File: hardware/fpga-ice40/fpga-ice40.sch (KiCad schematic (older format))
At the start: 70 parts, among them J1 MicroSD_Molex_1040310811, J4 Conn_02x20_Odd_Even, J5 USB_B_Micro, J6 Conn_02x05_Odd_Even, J7 Conn_02x05_Odd_Even, U1 iCE40HX4K-TQ144, U2 IS42S16320F-6TL, U3 W25Q32JVSS, U4 W25Q32JVSS, U5 S25FL256SAGMFI01, U6 S25FL256SAGMFI01, U7 FT245RL, U8 AZ1117-1.2, U9 AZ1117-1.2

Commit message: Oscillator, LEDs implemented, with all traces routed roughly
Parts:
- added C39, C40, C42: 10n, Capacitor_SMD:C_0603_1608Metric, symbol Device:C
- added C41, C43: 100n, Capacitor_SMD:C_0603_1608Metric, symbol Device:C
- added D2, D3, D4, D5, D6: Blue, LED_SMD:LED_0603_1608Metric, symbol Device:LED
- added FB1: 33R, 500mA, Inductor_SMD:L_0603_1608Metric, symbol Device:Ferrite_Bead
- added J2: Conn_01x03, Connector_PinHeader_2.54mm:PinHeader_1x03_P2.54mm_Vertical, symbol Connector_Generic:Conn_01x03
- added Q1: 2N7002H, Package_TO_SOT_SMD:SOT-23, symbol Transistor_FET:2N7002H
- added R5: 470R, Resistor_SMD:R_0603_1608Metric, symbol Device:R
- added R6: 100k, Resistor_SMD:R_0603_1608Metric, symbol Device:R
- added R7: 330R, Resistor_SMD:R_Array_Convex_4x0603, symbol Device:R_Pack04_Split
- added X1: ECS-2520MV-xxx-xx, Oscillator:Oscillator_SMD_ECS_2520MV-xxx-xx-4Pin_2.5x2.0mm, symbol Oscillator:ECS-2520MV-xxx-xx
- C27: footprint Capacitor_SMD:C_0603_1608Metric -> Capacitor_SMD:C_0805_2012Metric
- D1: value D_Schottky -> ~~800mVf; footprint (none) -> Diode_SMD:D_SOD-123
- RN4, RN5, RN6, RN7, RN8, RN9: value 33R0 -> 33R
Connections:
- net DRAM_DQ3: now also U1.2 (IOL_2B); no longer U1.141 (IOT_219)
- net DRAM_DQ4: now also U1.141 (IOT_219); no longer U1.2 (IOL_2B)
- net FIFO_D0: now also U1.105 (IOR_165); no longer U1.107 (IOR_167)
- net FIFO_D1: now also U1.101 (IOR_160); no longer U1.102 (IOR_161)
- net FIFO_D2: now also U1.102 (IOR_161); no longer U1.105 (IOR_165)
- net FIFO_D3: now also U1.94 (IOR_141_GBIN2); no longer U1.95 (IOR_144)
- net FIFO_D4: now also U1.104 (IOR_164); no longer U1.106 (IOR_166)
- net FIFO_D7: now also U1.99 (IOR_152); no longer U1.101 (IOR_160)
- net FIFO_RDn: now also U1.91 (IOR_139); no longer U1.94 (IOR_141_GBIN2)
- net FIFO_RXFn: now also U1.98 (IOR_148); no longer U1.104 (IOR_164)
- net FIFO_TXEn: now also U1.95 (IOR_144); no longer U1.99 (IOR_152)
- net FIFO_WR: now also U1.90 (IOR_138); no longer U1.93 (IOR_140_GBIN3)
- net FPGA_CDONE: now also Q1.1 (G)
- net GND: now also C39.2, C40.2, C41.2, C42.2, C43.2, D3.1 (K), D4.1 (K), D5.1 (K), D6.1 (K), Q1.2 (S), R6.1, X1.2 (GND)
- net N64_3V3: now also J2.1 (Pin_1)
- net N64_AD0_IC: now also U1.107 (IOR_167); no longer U1.112 (IOT_169)
- net N64_AD10_IC: now also U1.121 (IOT_181); no longer U1.128 (IOT_197_GBIN1)
- net N64_AD11_IC: now also U1.125 (IOT_192); no longer U1.124 (IOT_191)
- net N64_AD12_IC: now also U1.115 (IOT_172); no longer U1.117 (IOT_174)
- net N64_AD13_IC: now also U1.113 (IOT_170); no longer U1.115 (IOT_172)
- net N64_AD14_IC: now also U1.112 (IOT_169); no longer U1.110 (IOT_168)
- net N64_AD15_IC: now also U1.106 (IOR_166); no longer U1.113 (IOT_170)
- net N64_AD1_IC: now also U1.110 (IOT_168); no longer U1.114 (IOT_171)
- net N64_AD2_IC: now also U1.114 (IOT_171); no longer U1.116 (IOT_173)
- net N64_AD3_IC: now also U1.116 (IOT_173); no longer U1.118 (IOT_177)
- net N64_AD4_IC: now also U1.124 (IOT_191); no longer U1.125 (IOT_192)
- net N64_AD5_IC: now also U1.122 (IOT_190); no longer U1.129 (IOT_198_GBIN0)
- net N64_AD6: now also RN8.1 (R1.1); no longer RN8.2 (R2.1)
- net N64_AD6_IC: now also RN8.8 (R1.2), U1.130 (IOT_206); no longer RN8.7 (R2.2), U1.134 (IOT_212)
- net N64_AD7: now also RN8.3 (R3.1); no longer RN8.4 (R4.1)
- net N64_AD7_IC: now also RN8.6 (R3.2), U1.135 (IOT_213); no longer RN8.5 (R4.2), U1.136 (IOT_214)
- net N64_AD8: now also RN8.4 (R4.1); no longer RN8.3 (R3.1)
- net N64_AD8_IC: now also RN8.5 (R4.2), U1.136 (IOT_214); no longer RN8.6 (R3.2), U1.135 (IOT_213)
- net N64_AD9: now also RN8.2 (R2.1); no longer RN8.1 (R1.1)
- net N64_AD9_IC: now also RN8.7 (R2.2), U1.134 (IOT_212); no longer RN8.8 (R1.2), U1.130 (IOT_206)
- net N64_ALE_H_IC: now also U1.117 (IOT_174); no longer U1.122 (IOT_190)
- net N64_ALE_L: now also RN6.1 (R1.1); no longer RN6.2 (R2.1)
- net N64_ALE_L_IC: now also RN6.8 (R1.2); no longer RN6.7 (R2.2)
- net N64_COLD_RESETn: now also RN9.2 (R2.1); no longer RN9.1 (R1.1)
- net N64_COLD_RESETn_IC: now also RN9.7 (R2.2), U1.138 (IOT_216); no longer RN9.8 (R1.2), U1.137 (IOT_215)
- net N64_OS_EVENTn: now also RN9.1 (R1.1); no longer RN9.2 (R2.1)
- net N64_OS_EVENTn_IC: now also RN9.8 (R1.2), U1.137 (IOT_215); no longer RN9.7 (R2.2), U1.138 (IOT_216)
- net N64_READn_IC: now also U1.118 (IOT_177); no longer U1.121 (IOT_181)
- net N64_WRITEn: now also RN6.2 (R2.1); no longer RN6.1 (R1.1)
- net N64_WRITEn_IC: now also RN6.7 (R2.2); no longer RN6.8 (R1.2)
- net P3V3: now also C43.1, J2.2 (Pin_2), R5.1, X1.1 (Tri-State), X1.4 (VDD)
- net SD_CLK: now also U1.75 (IOR_111)
- net SD_CMD: now also RN3.3 (R3.1), U1.76 (IOR_112); no longer RN3.2 (R2.1)
- net SD_DAT0: now also RN3.2 (R2.1), U1.74 (IOR_110); no longer RN3.3 (R3.1)
- net SD_DAT1: now also RN3.1 (R1.1), U1.73 (IOR_109); no longer RN3.4 (R4.1)
- net SD_DAT2: now also U1.79 (IOR_115)
- net SD_DAT3: now also RN3.4 (R4.1), U1.78 (IOR_114); no longer RN3.1 (R1.1)
- net USB_3V3: now also J2.3 (Pin_3)
- net USB_DETn: now also U1.93 (IOR_140_GBIN3); no longer U1.98 (IOR_148)
- net USB_VBUS: now also C39.1, FB1.2; no longer C34.1, R3.1, U7.20 (VCC), U8.3 (VI)
- net SD_CD: now reaches U1.80 (IOR_116)
- net SD_CD: now also J1.9 (Pin_9)
- net LED_D0: now reaches U1.81 (IOR_117)
- net LED_D0: now also R7.5
- net LED_D1: now reaches U1.82 (IOR_118)
- net LED_D1: now also R7.6
- net LED_D2: now reaches U1.83 (IOR_119)
- net LED_D2: now also R7.7
- net LED_D3: now reaches U1.84 (IOR_120)
- net LED_D3: now also R7.8
- net USB_SHD: now reaches J5.6 (Shield)
- net USB_SHD: now also C42.1, R6.2
- new net: D2.1 (K), Q1.3 (D)
- new net: D2.2 (A), R5.2
- new net: D3.2 (A), R7.4
- new net: D6.2 (A), R7.1
- new net: D4.2 (A), R7.3
- new net: D5.2 (A), R7.2
- new net CLK_50MHZ: U1.128 (IOT_197_GBIN1), X1.3 (OUT)
- new net USB_5V: C34.1, C40.1, C41.1, FB1.1, R3.1, U7.20 (VCC), U8.3 (VI)
- no-connect marks 23 -> 29
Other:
- moved on the sheet: C33, C34, C35, C36, R3, R4, R9, U7, U8

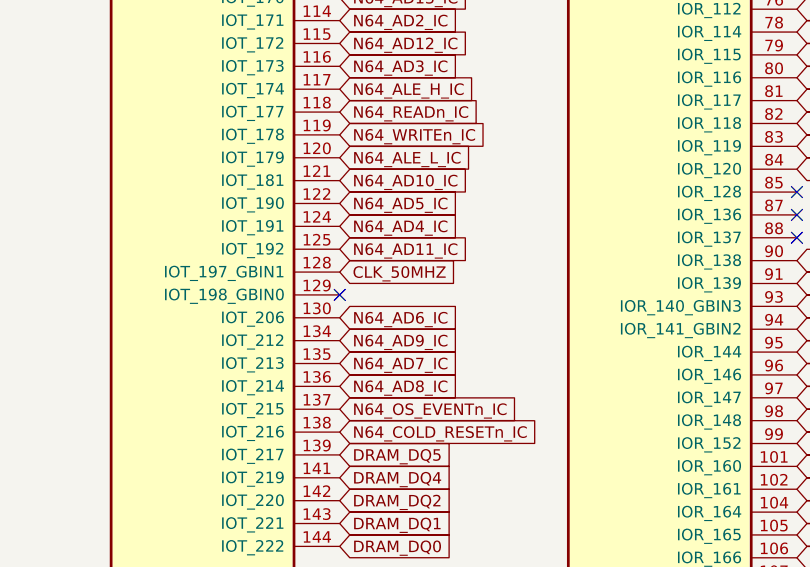
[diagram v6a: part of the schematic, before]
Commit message: Reroute N64 AD cart net away from clock oscillator output net
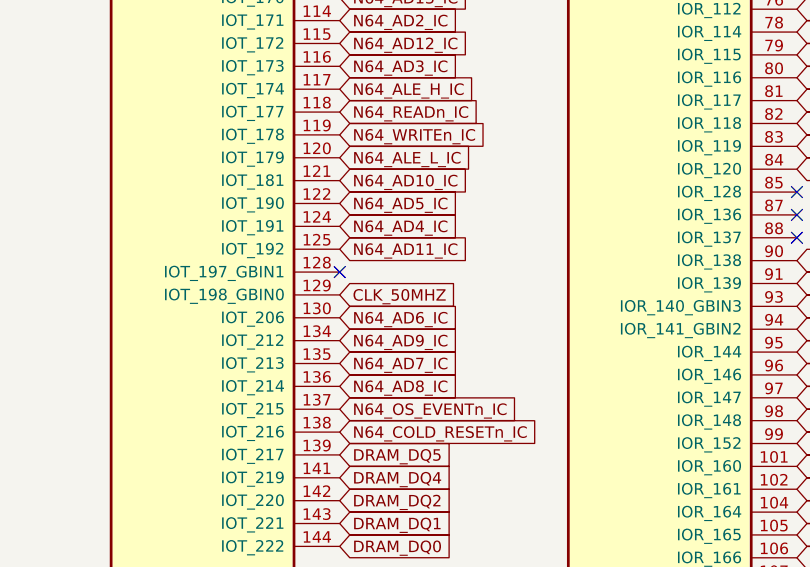
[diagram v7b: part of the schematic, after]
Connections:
- net CLK_50MHZ: now also U1.129 (IOT_198_GBIN0); no longer U1.128 (IOT_197_GBIN1)
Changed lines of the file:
@@
 Text GLabel 15200 3000 2    50   Input ~ 0
 CLK_50MHZ
-Text GLabel 2500 3000 2    50   Input ~ 0
+Text GLabel 2500 3100 2    50   Input ~ 0
 CLK_50MHZ
-NoConn ~ 2500 3100
+NoConn ~ 2500 3000
 NoConn ~ 4500 2650
 NoConn ~ 4500 2750

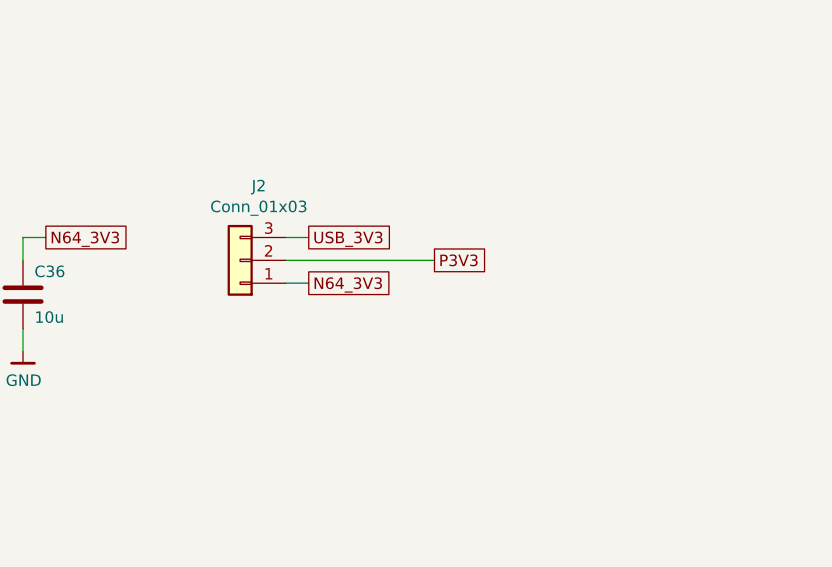
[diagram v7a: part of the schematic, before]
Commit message: Completed first pass routing with DRC checks passing
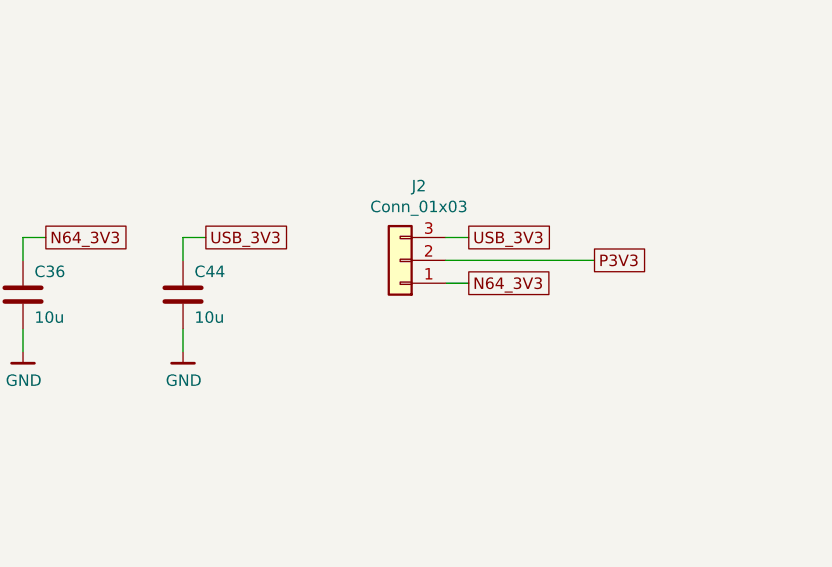
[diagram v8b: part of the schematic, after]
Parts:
- added C44: 10u, Capacitor_SMD:C_0805_2012Metric, symbol Device:C
- U3, U4: footprint Package_SO:SOIC-8_5.275x5.275mm_P1.27mm -> local_hacks:SOIC-8_5.275x5.275mm_P1.27mm__No_CrtYd
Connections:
- net GND: now also C44.2
- net USB_3V3: now also C44.1
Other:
- moved on the sheet: J2
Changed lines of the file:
@@
 F 0 "U3" H 18550 6750 50  0000 R CNN
 F 1 "W25Q32JVSS" H 18550 6650 50  0000 R CNN
-F 2 "Package_SO:SOIC-8_5.275x5.275mm_P1.27mm" H 18150 5750 50  0001 C CNN
+F 2 "local_hacks:SOIC-8_5.275x5.275mm_P1.27mm__No_CrtYd" H 18150 5750 50  0001 C CNN
 F 3 "https://www.mouser.com/datasheet/2/949/w25q32jv_dtr_revg_03272018_plus-1489786.pdf" H 18650 6300 50  0001 C CNN
 	1    17650 6600
@@
 F 0 "U4" H 18550 8850 50  0000 R CNN
 F 1 "W25Q32JVSS" H 18550 8750 50  0000 R CNN
-F 2 "Package_SO:SOIC-8_5.275x5.275mm_P1.27mm" H 18150 7850 50  0001 C CNN
+F 2 "local_hacks:SOIC-8_5.275x5.275mm_P1.27mm__No_CrtYd" H 18150 7850 50  0001 C CNN
 F 3 "https://www.mouser.com/datasheet/2/949/w25q32jv_dtr_revg_03272018_plus-1489786.pdf" H 18650 8400 50  0001 C CNN
 	1    17650 8700
@@
 L Connector_Generic:Conn_01x03 J2
 U 1 1 6261B7B7
-P 5050 11100
-F 0 "J2" H 4968 10775 50  0000 C CNN
-F 1 "Conn_01x03" H 4968 10866 50  0000 C CNN
-F 2 "Connector_PinHeader_2.54mm:PinHeader_1x03_P2.54mm_Vertical" H 5050 11100 50  0001 C CNN
-F 3 "~" H 5050 11100 50  0001 C CNN
-	1    5050 11100
+P 5750 11100
+F 0 "J2" H 5668 10775 50  0000 C CNN
+F 1 "Conn_01x03" H 5668 10866 50  0000 C CNN
+F 2 "Connector_PinHeader_2.54mm:PinHeader_1x03_P2.54mm_Vertical" H 5750 11100 50  0001 C CNN
+F 3 "~" H 5750 11100 50  0001 C CNN
+	1    5750 11100
 	-1   0    0    1
 $EndComp
 Wire Wire Line
-	5250 11000 5350 11000
-Wire Wire Line
-	5250 11100 5900 11100
-Wire Wire Line
-	5250 11200 5350 11200
-Text GLabel 5350 11000 2    50   UnSpc ~ 0
+	5950 11000 6050 11000
+Wire Wire Line
+	5950 11100 6600 11100
+Wire Wire Line
+	5950 11200 6050 11200
+Text GLabel 6050 11000 2    50   UnSpc ~ 0
 USB_3V3
-Text GLabel 5350 11200 2    50   UnSpc ~ 0
+Text GLabel 6050 11200 2    50   UnSpc ~ 0
 N64_3V3
-Text GLabel 5900 11100 2    50   UnSpc ~ 0
+Text GLabel 6600 11100 2    50   UnSpc ~ 0
 P3V3
+Text GLabel 4900 11000 2    50   UnSpc ~ 0
+USB_3V3
+Wire Wire Line
+	4900 11000 4800 11000
+Wire Wire Line
+	4800 11000 4800 11100
+$Comp
+L Device:C C44
+U 1 1 5EFFFC16
+P 4800 11250
+F 0 "C44" H 4850 11350 50  0000 L CNN
+F 1 "10u" H 4850 11150 50  0000 L CNN
+F 2 "Capacitor_SMD:C_0805_2012Metric" H 4838 11100 50  0001 C CNN
+F 3 "~" H 4800 11250 50  0001 C CNN
+	1    4800 11250
+	1    0    0    -1
+$EndComp
+Wire Wire Line
+	4800 11400 4800 11500
+$Comp
+L ng_power:GND #PWR0113
+U 1 1 5EFFFC21
+P 4800 11500
+F 0 "#PWR0113" H 4800 11250 50  0001 C CNN
+F 1 "GND" H 4803 11374 50  0000 C CNN
+F 2 "" H 4700 11150 50  0001 C CNN
+F 3 "" H 4800 11500 50  0001 C CNN
+	1    4800 11500
+	1    0    0    -1
+$EndComp
 $EndSCHEMATC
